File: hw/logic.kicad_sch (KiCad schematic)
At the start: 29 parts, among them J5 JTAG, J6 UART, J7 Conn_01x05_Socket, SW2 SW_Push, SW3 SW_Push, U7 XGZP6897D, U8 SC7A20, U9 ESP32-C6-MINI-1/U, Y1 32.768k

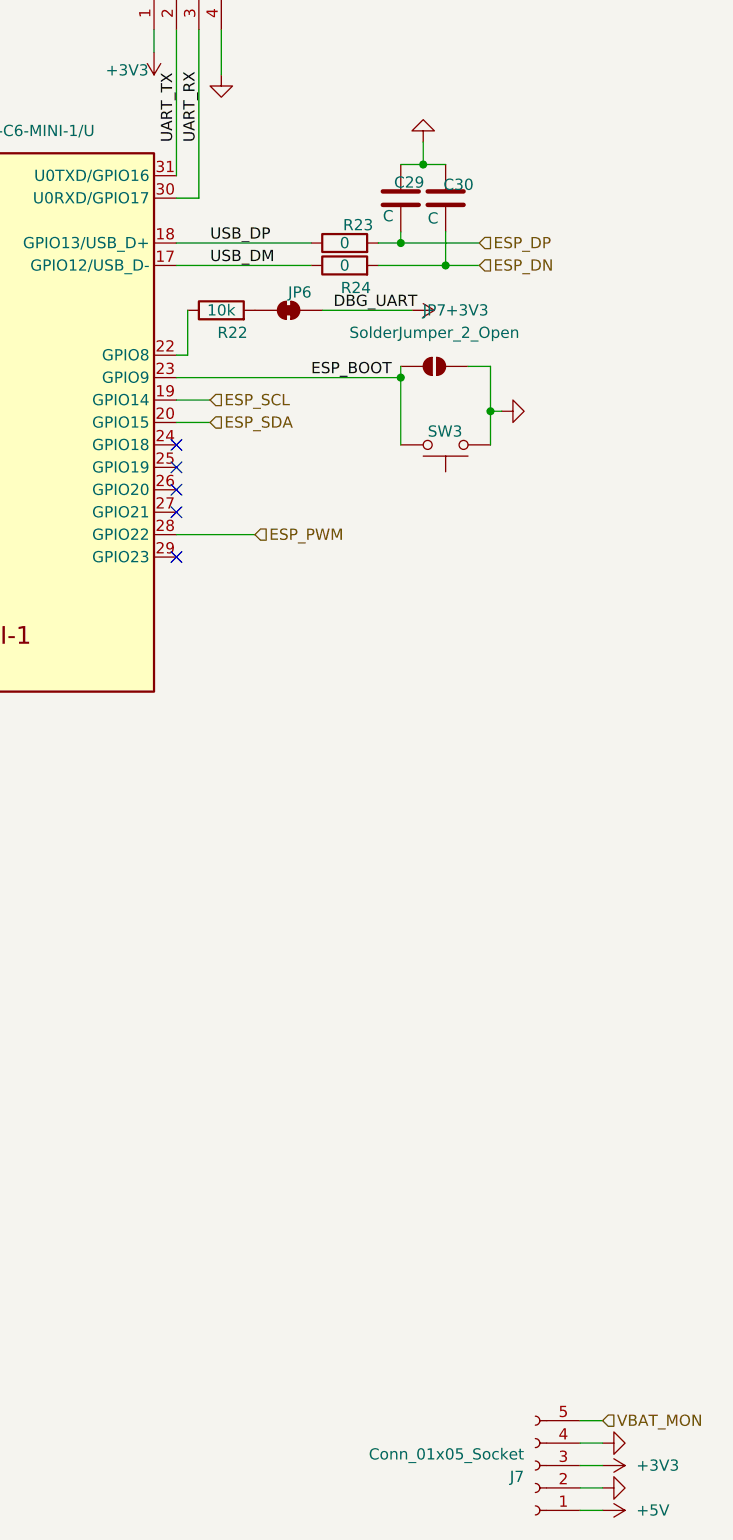
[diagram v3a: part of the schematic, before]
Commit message: Footprinting, begin layout
I've assigned all the footprints except a few, so I've started on layout.
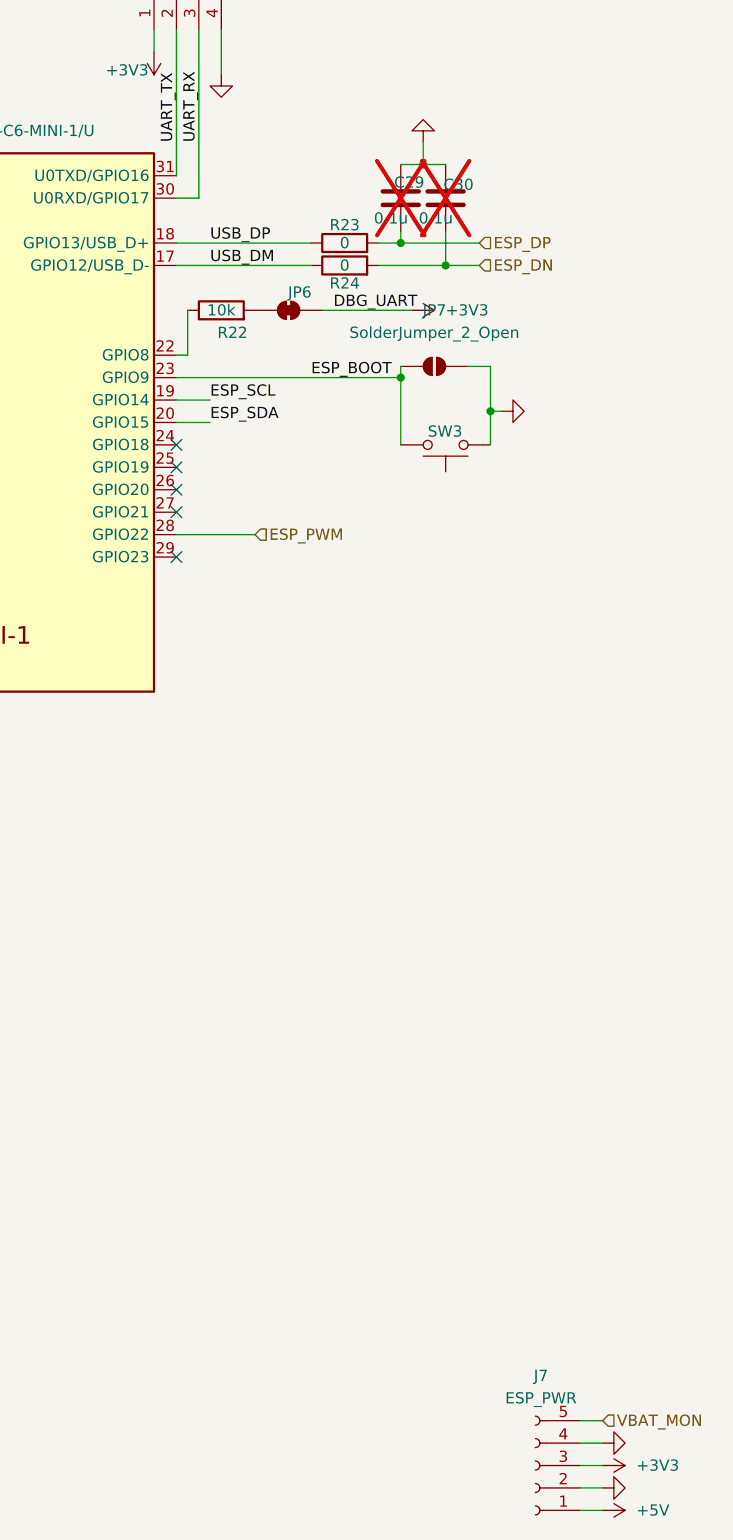
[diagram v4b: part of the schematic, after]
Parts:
- C23, C24, C25, C26, C28: footprint Capacitor_SMD:C_0603_1608Metric -> Capacitor_SMD:C_0402_1005Metric
- C27: footprint Capacitor_SMD:C_1206_3216Metric -> Capacitor_SMD:C_0805_2012Metric
- C29, C30: value C -> 0.1u; footprint (none) -> Capacitor_SMD:C_0603_1608Metric; now not fitted
- J5: footprint Connector_JST:JST_EH_B4B-EH-A_1x04_P2.50mm_Vertical -> Connector_JST:JST_ZH_B4B-ZR_1x04_P1.50mm_Vertical
- J6: footprint Connector_JST:JST_XH_B4B-XH-A_1x04_P2.50mm_Vertical -> Connector_JST:JST_ZH_B4B-ZR_1x04_P1.50mm_Vertical
- J7: value Conn_01x05_Socket -> ESP_PWR; footprint Connector_JST:JST_EH_B5B-EH-A_1x05_P2.50mm_Vertical -> Connector_JST:JST_ZH_B5B-ZR_1x05_P1.50mm_Vertical
- R15, R16, R21, R22: footprint (none) -> Resistor_SMD:R_0603_1608Metric
- R17, R18, R19, R20, R23, R24: footprint PCM_Resistor_SMD_AKL:R_0805_2012Metric -> Resistor_SMD:R_0603_1608Metric
- SW2, SW3: footprint Button_Switch_THT:SW_Tactile_SPST_Angled_PTS645Vx31-2LFS -> Button_Switch_SMD:SW_SPST_CK_RS282G05A3
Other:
- title: (none) -> Weltkatze
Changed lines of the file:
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@@
 	(generator_version "8.0")
 	(paper "A4")
+	(title_block
+		(title "Weltkatze")
+		(date "2025-02-25")
+		(rev "1")
+	)
 	(junction
 		(at 87.63 30.48)
@@
 		)
 	)
+	(label "ESP_SDA"
+		(at 119.38 69.85 0)
+		(effects
+			(font
+				(size 1.27 1.27)
+			)
+			(justify left bottom)
+		)
+	)
 	(label "UART_RX"
 		(at 118.11 38.1 90)
@@
 		)
 	)
+	(label "ESP_SCL"
+		(at 119.38 67.31 0)
+		(effects
+			(font
+				(size 1.27 1.27)
+			)
+			(justify left bottom)
+		)
+	)
 	(label "XTAL_N"
 		(at 58.42 49.53 180)
@@
 		)
 	)
-	(hierarchical_label "ESP_SDA"
-		(shape input)
-		(at 119.38 69.85 0)
-		(effects
-			(font
-				(size 1.27 1.27)
-			)
-			(justify left)
-		)
-	)
-	(hierarchical_label "ESP_SCL"
-		(shape input)
-		(at 119.38 67.31 0)
-		(effects
-			(font
-				(size 1.27 1.27)
-			)
-			(justify left)
-		)
-	)
 	(hierarchical_label "VBAT_MON"
 		(shape input)
@@
 			)
 		)
-		(property "Footprint" "Capacitor_SMD:C_1206_3216Metric"
+		(property "Footprint" "Capacitor_SMD:C_0805_2012Metric"
 			(at 85.09 29.5148 0)
 			(effects
@@
 			)
 		)
-		(property "Footprint" "Capacitor_SMD:C_0603_1608Metric"
+		(property "Footprint" "Capacitor_SMD:C_0402_1005Metric"
 			(at 52.07 24.4348 0)
 			(effects
@@
 		(dnp no)
 		(property "Reference" "R23"
-			(at 136.144 47.498 90)
+			(at 134.62 47.498 90)
 			(effects
 				(font
@@
 			)
 		)
-		(property "Footprint" "PCM_Resistor_SMD_AKL:R_0805_2012Metric"
+		(property "Footprint" "Resistor_SMD:R_0603_1608Metric"
 			(at 134.62 51.308 90)
 			(effects
@@
 			)
 		)
-		(property "Footprint" "Capacitor_SMD:C_0603_1608Metric"
+		(property "Footprint" "Capacitor_SMD:C_0402_1005Metric"
 			(at 30.48 43.4848 0)
 			(effects
@@
 			)
 		)
-		(property "Footprint" ""
+		(property "Footprint" "Resistor_SMD:R_0603_1608Metric"
 			(at 31.75 62.992 90)
 			(effects
@@
 			)
 		)
-		(property "Footprint" "Capacitor_SMD:C_0603_1608Metric"
+		(property "Footprint" "Capacitor_SMD:C_0402_1005Metric"
 			(at 48.26 42.8752 0)
 			(effects
@@
 			)
 		)
-		(property "Footprint" "PCM_Resistor_SMD_AKL:R_0805_2012Metric"
+		(property "Footprint" "Resistor_SMD:R_0603_1608Metric"
 			(at 46.99 48.768 90)
 			(effects
@@
 			)
 		)
-		(property "Footprint" ""
+		(property "Footprint" "Resistor_SMD:R_0603_1608Metric"
 			(at 120.65 58.928 90)
 			(effects
@@
 			)
 		)
-		(property "Footprint" "Connector_JST:JST_EH_B4B-EH-A_1x04_P2.50mm_Vertical"
+		(property "Footprint" "Connector_JST:JST_ZH_B4B-ZR_1x04_P1.50mm_Vertical"
 			(at 50.8 67.31 0)
 			(effects
@@
 			)
 		)
-		(property "Footprint" "Button_Switch_THT:SW_Tactile_SPST_Angled_PTS645Vx31-2LFS"
+		(property "Footprint" "Button_Switch_SMD:SW_SPST_CK_RS282G05A3"
 			(at 146.05 77.47 0)
 			(effects
@@
 		(fields_autoplaced yes)
 		(property "Reference" "J7"
-			(at 154.94 189.2301 0)
+			(at 156.845 177.8 0)
 			(effects
 				(font
 					(size 1.27 1.27)
 				)
-				(justify left)
 			)
 		)
-		(property "Value" "Conn_01x05_Socket"
-			(at 154.94 186.6901 0)
+		(property "Value" "ESP_PWR"
+			(at 156.845 180.34 0)
 			(effects
 				(font
 					(size 1.27 1.27)
 				)
-				(justify left)
 			)
 		)
-		(property "Footprint" "Connector_JST:JST_EH_B5B-EH-A_1x05_P2.50mm_Vertical"
+		(property "Footprint" "Connector_JST:JST_ZH_B5B-ZR_1x05_P1.50mm_Vertical"
 			(at 156.21 187.96 0)
 			(effects
@@
 			)
 		)
-		(property "Footprint" "Capacitor_SMD:C_0603_1608Metric"
+		(property "Footprint" "Capacitor_SMD:C_0402_1005Metric"
 			(at 30.48 51.1048 0)
 			(effects
@@
 			)
 		)
-		(property "Footprint" "Button_Switch_THT:SW_Tactile_SPST_Angled_PTS645Vx31-2LFS"
+		(property "Footprint" "Button_Switch_SMD:SW_SPST_CK_RS282G05A3"
 			(at 48.26 15.24 0)
 			(effects
@@
 			)
 		)
-		(property "Footprint" "PCM_Resistor_SMD_AKL:R_0805_2012Metric"
+		(property "Footprint" "Resistor_SMD:R_0603_1608Metric"
 			(at 46.99 51.308 90)
 			(effects
@@
 			)
 		)
-		(property "Footprint" "PCM_Resistor_SMD_AKL:R_0805_2012Metric"
+		(property "Footprint" "Resistor_SMD:R_0603_1608Metric"
 			(at 41.148 48.26 90)
 			(effects
@@
 			)
 		)
-		(property "Footprint" ""
+		(property "Footprint" "Resistor_SMD:R_0603_1608Metric"
 			(at 66.04 30.988 90)
 			(effects
@@
 		(in_bom yes)
 		(on_board yes)
-		(dnp no)
+		(dnp yes)
 		(property "Reference" "C29"
 			(at 140.208 42.672 0)
@@
 			)
 		)
-		(property "Value" "C"
-			(at 138.938 46.482 0)
+		(property "Value" "0.1u"
+			(at 137.922 46.736 0)
 			(effects
 				(font
@@
 			)
 		)
-		(property "Footprint" ""
+		(property "Footprint" "Capacitor_SMD:C_0603_1608Metric"
 			(at 141.9352 48.26 0)
 			(effects
@@
 			)
 		)
-		(property "Footprint" "Connector_JST:JST_XH_B4B-XH-A_1x04_P2.50mm_Vertical"
+		(property "Footprint" "Connector_JST:JST_ZH_B4B-ZR_1x04_P1.50mm_Vertical"
 			(at 115.57 20.32 0)
 			(effects
@@
 			)
 		)
-		(property "Footprint" "PCM_Resistor_SMD_AKL:R_0805_2012Metric"
+		(property "Footprint" "Resistor_SMD:R_0603_1608Metric"
 			(at 61.468 24.13 90)
 			(effects
@@
 			)
 		)
-		(property "Footprint" ""
+		(property "Footprint" "Resistor_SMD:R_0603_1608Metric"
 			(at 39.878 68.58 90)
 			(effects
@@
 		(in_bom yes)
 		(on_board yes)
-		(dnp no)
+		(dnp yes)
 		(property "Reference" "C30"
 			(at 145.796 42.926 0)
@@
 			)
 		)
-		(property "Value" "C"
-			(at 144.018 46.736 0)
+		(property "Value" "0.1u"
+			(at 143.002 46.736 0)
 			(effects
 				(font
@@
 			)
 		)
-		(property "Footprint" ""
+		(property "Footprint" "Capacitor_SMD:C_0603_1608Metric"
 			(at 147.0152 48.26 0)
 			(effects
@@
 		(dnp no)
 		(property "Reference" "R24"
-			(at 135.89 54.61 90)
+			(at 134.62 54.102 90)
 			(effects
 				(font
@@
 			)
 		)
-		(property "Footprint" "PCM_Resistor_SMD_AKL:R_0805_2012Metric"
+		(property "Footprint" "Resistor_SMD:R_0603_1608Metric"
 			(at 134.62 53.848 90)
 			(effects
@@
 			)
 		)
-		(property "Footprint" "Capacitor_SMD:C_0603_1608Metric"
+		(property "Footprint" "Capacitor_SMD:C_0402_1005Metric"
 			(at 85.09 34.5948 0)
 			(effects

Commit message: Rest of the owl
Finish major layout, minor tweaks can be made
E.g. rotating the LEDs so they look pretty

Still need to make it so the inner PCB is manufacturable
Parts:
- removed J5: JTAG, Connector_JST:JST_ZH_B4B-ZR_1x04_P1.50mm_Vertical, symbol Connector:Conn_01x04_Socket
- removed U7: XGZP6897D, Sensor_Pressure:CFSensor_XGZP6897x, symbol Sensor_Pressure:XGZP6897D
- removed U8: SC7A20, Package_LGA:LGA-12_2x2mm_P0.5mm, symbol Sensor_Motion:SC7A20
- added C31, C33, C34, C35: 100n, Capacitor_SMD:C_0402_1005Metric, symbol Device:C
- added C32: 10u, Capacitor_SMD:C_0603_1608Metric, symbol Device:C
- added JP9: SolderJumper_2_Open, Jumper:SolderJumper-2_P1.3mm_Open_TrianglePad1.0x1.5mm, symbol Jumper:SolderJumper_2_Open
- added TP1: MTMS, TestPoint:TestPoint_Pad_D1.0mm, symbol Connector:TestPoint_Small
- added TP2: MTDI, TestPoint:TestPoint_Pad_D1.0mm, symbol Connector:TestPoint_Small
- added TP3: MTCK, TestPoint:TestPoint_Pad_D1.0mm, symbol Connector:TestPoint_Small
- added TP4: MTDO, TestPoint:TestPoint_Pad_D1.0mm, symbol Connector:TestPoint_Small
- added TP5: 3V3, TestPoint:TestPoint_Pad_D1.0mm, symbol Connector:TestPoint_Small
- added U7: BMP280, Package_LGA:Bosch_LGA-8_2x2.5mm_P0.65mm_ClockwisePinNumbering, symbol Sensor_Pressure:BMP280
- added U8: LSM303C, Package_LGA:LGA-12_2x2mm_P0.5mm, symbol Sensor_Motion:LSM303C
- J7: footprint Connector_JST:JST_ZH_B5B-ZR_1x05_P1.50mm_Vertical -> Connector_JST:JST_ZH_B6B-ZR_1x06_P1.50mm_Vertical; symbol Connector:Conn_01x05_Socket -> Connector:Conn_01x06_Socket
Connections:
- net +3V3: now also C31.1, C32.1, C33.1, C34.1, C35.1, JP9.2 (B), TP5.1, U7.2 (CSB), U7.6 (VDDIO), U7.8 (VDD), U8.10 (VDDIO), U8.2 (CS_XL), U8.9 (VDD); no longer J7.3 (Pin_3)
- net +5V: now also J7.4 (Pin_4); no longer J7.1 (Pin_1)
- net ESP_SCL: now also U7.4 (SCK), U8.1 (SCL/SPC)
- net ESP_SDA: now also U7.3 (SDI), U8.4 (SDA/SDI/SDO)
- net GND: now also J7.3 (Pin_3), J7.5 (Pin_5), C31.2, C32.2, C33.2, C34.2, C35.2, U7.1 (GND), U7.5 (SDO), U7.7 (GND), U8.6 (GND), U8.8 (GND); no longer J7.2 (Pin_2), J7.4 (Pin_4)
- net UART_RX: now also J6.2 (Pin_2); no longer J6.3 (Pin_3)
- net UART_TX: now also J6.3 (Pin_3); no longer J6.2 (Pin_2)
- net VBAT_MON: now also J7.6 (Pin_6); no longer J7.5 (Pin_5), R15.2
- net XTAL_N: now also R18.2; no longer R19.2
- net XTAL_P: now also R19.2; no longer R18.2
- net at U9.10 (MTDI/GPIO5/ADC1_CH5): now also TP2.1
- net at U9.15 (MTCK/GPIO6/ADC1_CH6): now also TP3.1
- net at U9.16 (MTDO/GPIO7): now also TP4.1
- net at U9.9 (MTMS/GPIO4/ADC1_CH4): now also TP1.1
- net ESP_DN renamed USBD_N
- net USBD_N: now also J7.2 (Pin_2)
- net ESP_DP renamed USBD_P
- net USBD_P: now also J7.1 (Pin_1)
- net USB_DM: no longer names the net of R24.1, U9.17 (GPIO12/USB_D-)
- net USB_DP: no longer names the net of R23.1, U9.18 (GPIO13/USB_D+)
- new net: JP9.1 (A), U8.3 (CS_MAG)
- new net VBAT: R15.2
- no-connect marks 22 -> 6
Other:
- note added: "ESP32-C6"
- note added: "Sensor package Accel+mag Baro"
- moved on the sheet: J6

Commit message: V1 REV1 Final!
I consider this design finished, as such I've submitted it to JLCPCB

I converted to a 6L pcb because its cheaper, in.3 and in.4 have no copper
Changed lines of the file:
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@@
-		)
-	)
-	(label "USBD_N"
-		(at 166.37 193.04 0)
-		(effects
-			(font
-				(size 1.27 1.27)
-			)
-			(justify left bottom)
 		)
 	)
@@
 		)
 	)
-	(label "USBD_P"
-		(at 166.37 195.58 0)
-		(effects
-			(font
-				(size 1.27 1.27)
-			)
-			(justify left bottom)
-		)
-	)
 	(label "VBAT_MON"
 		(at 43.18 64.77 90)
@@
 		)
 	)
+	(hierarchical_label "USBD_N"
+		(shape input)
+		(at 166.37 193.04 0)
+		(effects
+			(font
+				(size 1.27 1.27)
+			)
+			(justify left)
+		)
+	)
 	(hierarchical_label "ESP_PWM"
 		(shape input)
@@
 		(effects
 			(font
+				(size 1.27 1.27)
+			)
+			(justify left)
+		)
+	)
+	(hierarchical_label "USBD_P"
+		(shape input)
+		(at 166.37 195.58 0)
+		(effects
+			(font

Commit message: Minor reroute
Minor reroute of traces, utilises all 6 layers effectively now.
Also reduces some issues with USB going through multiple layers unnecessarily
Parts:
- C29, C30: now left out of the parts list
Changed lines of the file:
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@@
 		(unit 1)
 		(exclude_from_sim no)
-		(in_bom yes)
+		(in_bom no)
 		(on_board yes)
 		(dnp yes)
@@
 		(unit 1)
 		(exclude_from_sim no)
-		(in_bom yes)
+		(in_bom no)
 		(on_board yes)
 		(dnp yes)
